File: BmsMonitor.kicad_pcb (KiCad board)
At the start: 2 copper layers, 65.5 x 98 mm, 9 parts, among them J1 Conn_01x03, J2 Conn_01x03, J3 Conn_01x04, J4 Conn_01x22, J5 Conn_01x22, U1 2365-DC-DC module, U2 ESP32-S3-DevKitC, U3 TJA1050 Module, U4 Open-Smart_3.8_LCD

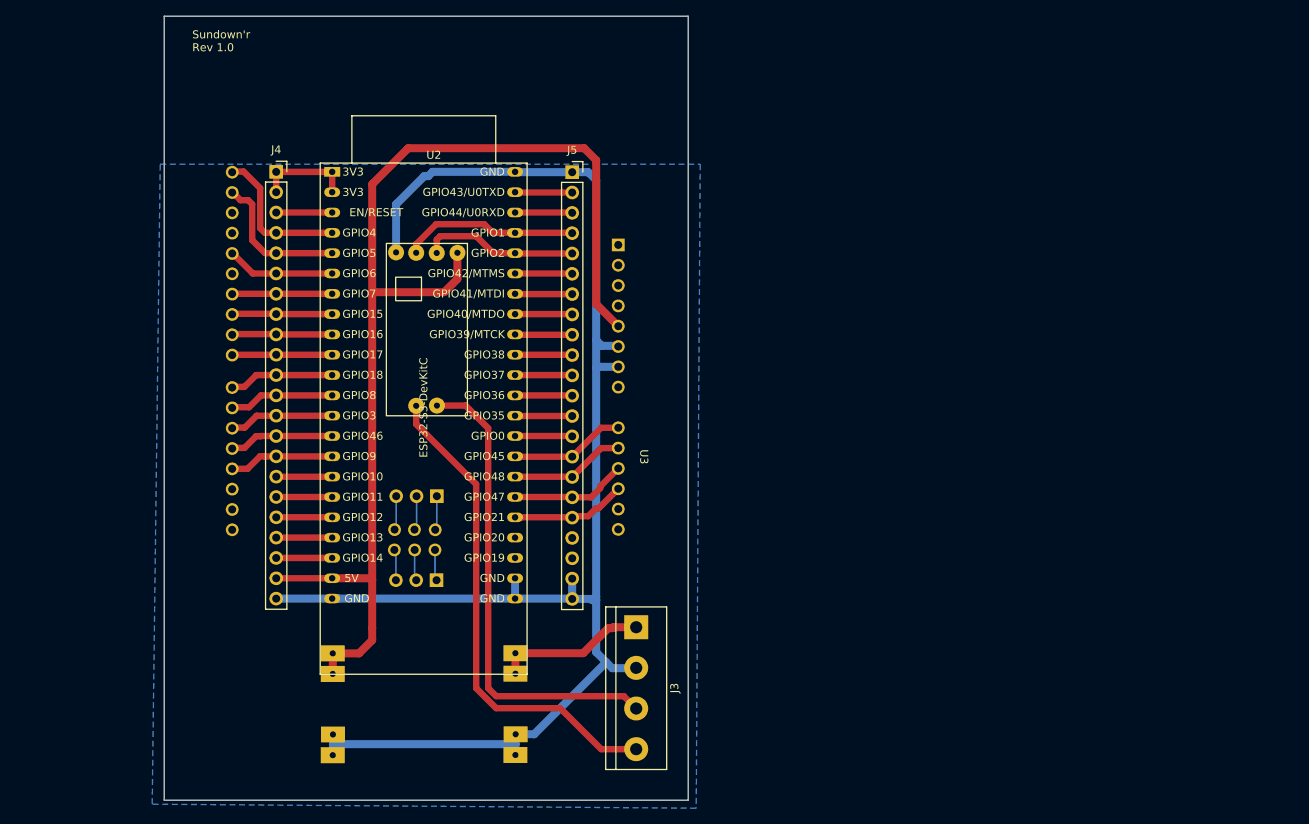
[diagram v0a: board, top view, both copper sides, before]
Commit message: BmsMonitor Ver 2.0
Changed to work with Display having a SPI variant of ILI9488
as well as a XPT2046 touch controller.

The display in question is this 3.5" display:
https://www.aliexpress.com/item/33057812377.html
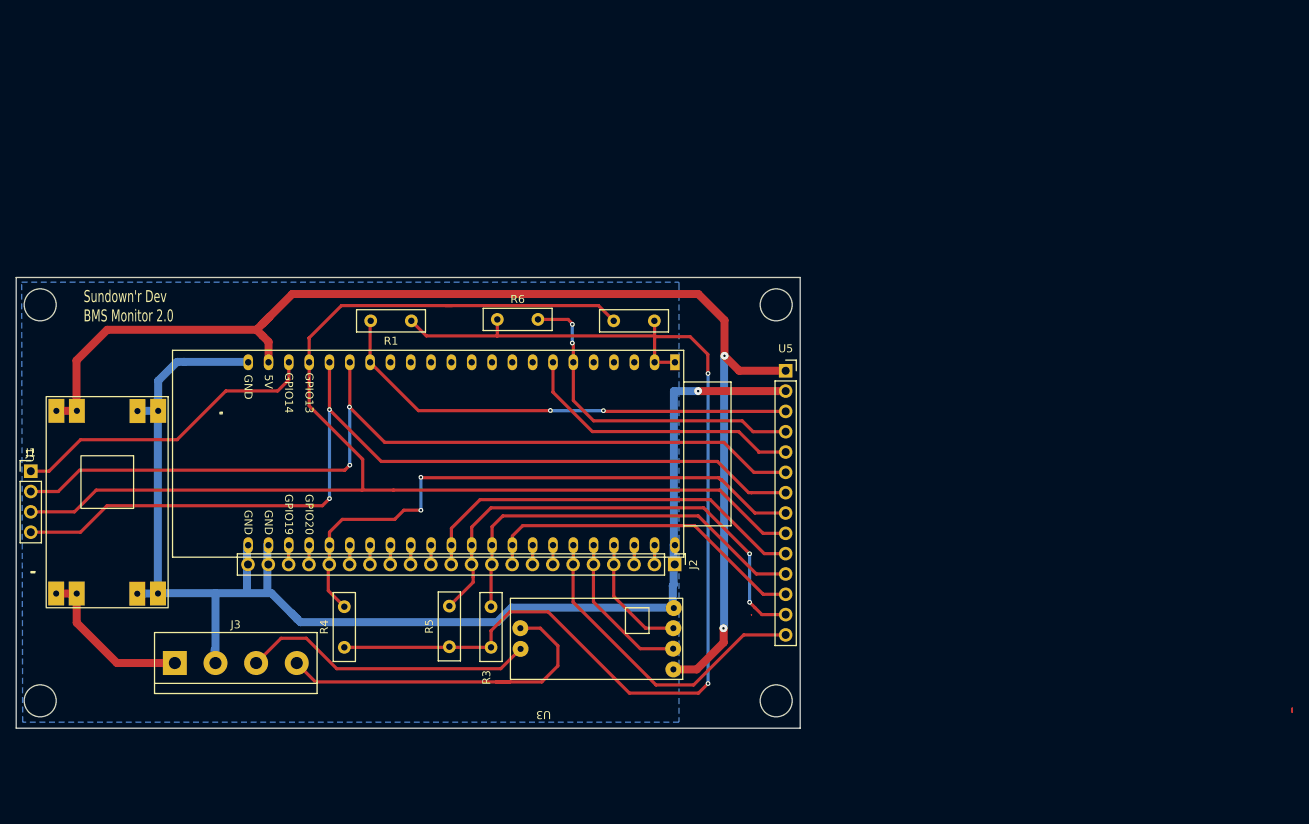
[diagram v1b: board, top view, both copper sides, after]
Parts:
- removed J4, J5: Conn_01x22, Connector_PinSocket_2.54mm:PinSocket_1x22_P2.54mm_Vertical
- removed U4: Open-Smart_3.8_LCD, Private:Open_smart_3.8_LCD
- added R1: 10K, Resistor_THT:R_Box_L8.4mm_W2.5mm_P5.08mm, F.Cu at (147.4, 68.6)
- added R2: 10K, Resistor_THT:R_Box_L8.4mm_W2.5mm_P5.08mm, F.Cu at (177.8, 68.6)
- added R3: 10K, Resistor_THT:R_Box_L8.4mm_W2.5mm_P5.08mm, F.Cu at (157.4, 109.4)
- added R4: 10K, Resistor_THT:R_Box_L8.4mm_W2.5mm_P5.08mm, F.Cu at (139.0, 109.4)
- added R5: 10K, Resistor_THT:R_Box_L8.4mm_W2.5mm_P5.08mm, F.Cu at (152.1, 109.3)
- added R6: 10K, Resistor_THT:R_Box_L8.4mm_W2.5mm_P5.08mm, F.Cu at (158.1, 68.4)
- added U5: LCD_3.5_TFT_SPI_480x320, Connector_PinSocket_2.54mm:PinSocket_1x14_P2.54mm_Vertical, F.Cu at (194.2, 74.8)
- J1: value Conn_01x03 -> Conn_01x04; footprint Connector_PinHeader_2.54mm:PinHeader_1x03_P2.54mm_Vertical -> Connector_PinHeader_2.54mm:PinHeader_1x04_P2.54mm_Vertical; moved to F.Cu
- J2: value Conn_01x03 -> Conn_01x22; footprint Connector_PinHeader_2.54mm:PinHeader_1x03_P2.54mm_Vertical -> Connector_PinHeader_2.54mm:PinHeader_1x22_P2.54mm_Vertical; moved to F.Cu
- U1: moved to F.Cu
- moved J3 57.8 mm to (117.8, 111.4), turned to 0 degrees
- moved J1 52.5 mm to (99.8, 87.4), turned to 0 degrees
- moved U2 49.0 mm to (180.3, 73.8), turned to -90 degrees
- moved U1 47.0 mm to (109.4, 91.3), turned to 90 degrees
- moved J2 30.9 mm to (180.3, 99.0), turned to -90 degrees
- moved U3 22.5 mm to (154.7, 107.0), turned to 180 degrees
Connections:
- J1 pad 1: Net-(J1-Pin_1) -> SD_CS
- J1 pad 2: Net-(J1-Pin_2) -> LCD_MOSI
- J1 pad 3: Net-(J1-Pin_3) -> LCD_MISO
- J2 pad 1: Net-(J2-Pin_1) -> GND
- U2 pad 10: LCD_D0 -> unconnected-(U2-GPIO17/ADC2_CH6-Pad10)
- U2 pad 11: LCD_D7 -> unconnected-(U2-GPIO18/ADC2_CH7-Pad11)
- U2 pad 12: LCD_D6 -> unconnected-(U2-GPIO8/ADC1_CH7-Pad12)
- U2 pad 13: SD_CS -> unconnected-(U2-GPIO3/ADC1_CH2-Pad13)
- U2 pad 14: LCD_D4 -> unconnected-(U2-GPIO46-Pad14)
- U2 pad 15: Backlight -> unconnected-(U2-GPIO9/ADC1_CH8-Pad15)
- U2 pad 16: GPIO10 -> LCD_CS
- U2 pad 17: GPIO11 -> LCD_MOSI
- U2 pad 18: GPIO12 -> LCD_CLK
- U2 pad 19: GPIO13 -> LCD_MISO
- U2 pad 20: GPIO14 -> SD_CS
- U2 pad 25: unconnected-(U2-GPIO19/USB_D--Pad25) -> unconnected-(J2-Pin_20-Pad20)
- U2 pad 26: unconnected-(U2-GPIO20/USB_D+-Pad26) -> unconnected-(J2-Pin_19-Pad19)
- U2 pad 27: LCD_CS -> Backlight
- U2 pad 28: LCD_RS -> GPIO47
- U2 pad 29: LCD_WR -> GPIO48
- U2 pad 30: LCD_RD -> GPIO45
- U2 pad 33: GPIO36 -> T_CLK
- U2 pad 34: GPIO37 -> T_MISO
- U2 pad 35: GPIO38 -> T_CS
- U2 pad 36: GPIO39 -> T_MOSI
- U2 pad 39: GPIO42 -> T_IRQ
- U2 pad 4: SCL -> unconnected-(U2-GPIO4/ADC1_CH3-Pad4)
- U2 pad 42: GPIO44 -> Net-(J2-Pin_3)
- U2 pad 43: GPIO43 -> Net-(J2-Pin_2)
- U2 pad 5: SDA -> unconnected-(U2-GPIO5/ADC1_CH4-Pad5)
- U2 pad 6: LCD_D5 -> LCD_RESET
- U2 pad 7: LCD_D3 -> LCD_DC/RS
- U2 pad 8: LCD_D2 -> unconnected-(U2-GPIO15/ADC2_CH4/32K_P-Pad8)
- U2 pad 9: LCD_D1 -> unconnected-(U2-GPIO16/ADC2_CH5/32K_N-Pad9)
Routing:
- net LCD_MISO: track 0.00 -> 161.0 mm
- net +3V3: track 12.1 -> 142.9 mm, vias 0 -> 2
- net LCD_CLK: track 0.00 -> 117.4 mm, vias 0 -> 2
- net LCD_MOSI: track 0.00 -> 112.1 mm, vias 0 -> 2
- net Backlight: track 13.2 -> 74.2 mm, vias 0 -> 2
- net T_MISO: track 0.00 -> 60.5 mm, vias 0 -> 2
- net T_CLK: track 0.00 -> 50.6 mm
- net T_CS: track 0.00 -> 50.3 mm
- net LCD_CS: track 14.5 -> 59.8 mm, vias 0 -> 2
- net LCD_RESET: track 0.00 -> 42.3 mm, vias 0 -> 2
- net T_MOSI: track 0.00 -> 41.8 mm
- net T_IRQ: track 0.00 -> 40.6 mm
- net LCD_DC/RS: track 0.00 -> 36.0 mm
- net SD_CS: track 13.2 -> 39.2 mm
- net CAN_H: track 59.6 -> 36.9 mm
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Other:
- board size 65.5 x 98 mm -> 98 x 56.3 mm
- board text added: "Sundown'r Dev BMS Monitor 2.0"
- board text added: "Sundown'r Dev BMS Monitor rev. 2.0"
- board text removed: "Sundown'r Rev 1.0"

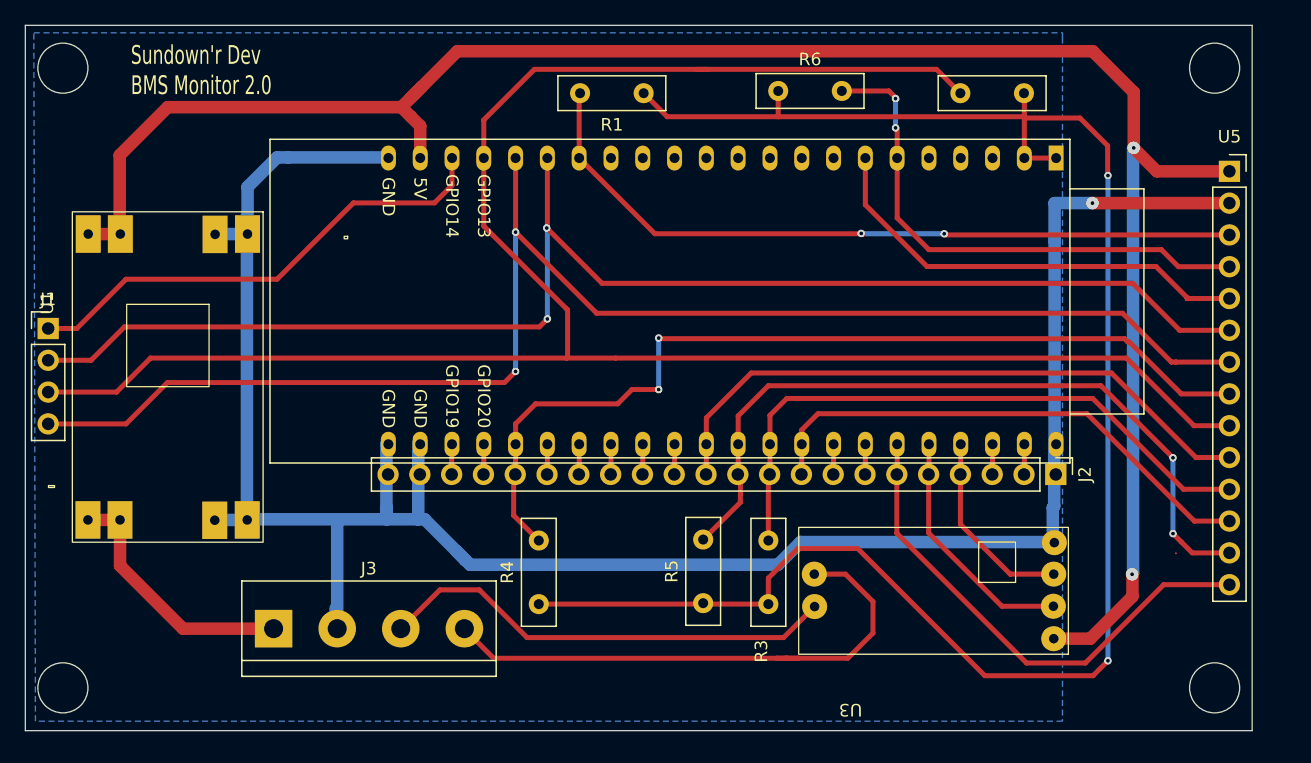
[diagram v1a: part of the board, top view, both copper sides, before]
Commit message: Use common SPI for both display and touch.
Added M12 connector for possible power and CAN
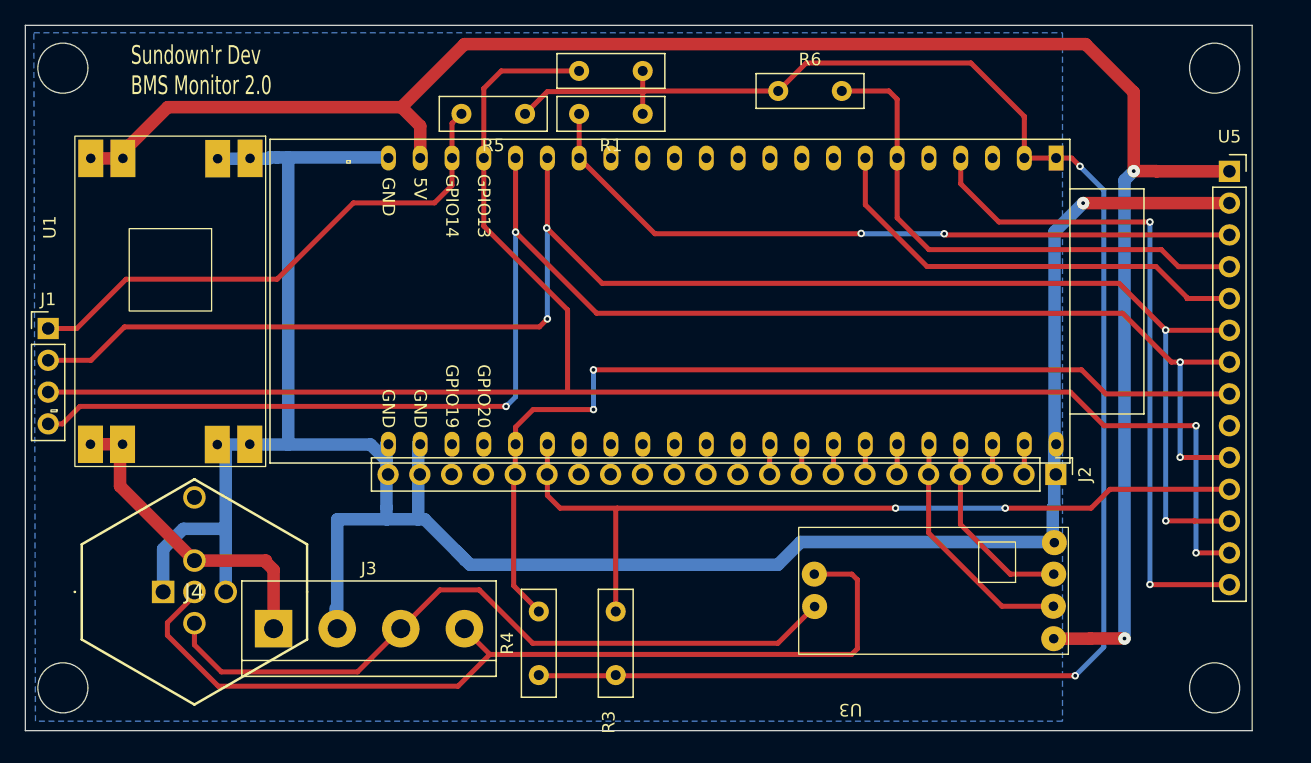
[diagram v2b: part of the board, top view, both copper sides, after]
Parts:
- added J4: MI5K101-400-A0-05, KiCad:MI5K101400A005, F.Cu at (109.0, 108.4)
- moved R5 41.6 mm to (137.9, 70.2), turned to 180 degrees
- moved R2 30.5 mm to (147.3, 66.8)
- moved R3 13.4 mm to (145.2, 115.1)
- moved U1 6.05 mm to (109.6, 85.2)
- moved R4 5.67 mm to (139.0, 115.1)
- moved R1 1.65 mm to (147.3, 70.2)
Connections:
- net GPIO40 renamed MTDO
- net GPIO41 renamed MTDI
- J2 pad 10: T_CS -> 3col_LED
- J2 pad 11: T_MISO -> unconnected-(J2-Pin_11-Pad11)
- J2 pad 12: T_CLK -> unconnected-(J2-Pin_12-Pad12)
- J2 pad 13: GPIO35 -> unconnected-(J2-Pin_13-Pad13)
- J2 pad 14: GPIO0 -> unconnected-(J2-Pin_14-Pad14)
- J2 pad 15: GPIO45 -> unconnected-(J2-Pin_15-Pad15)
- J2 pad 16: GPIO48 -> unconnected-(J2-Pin_16-Pad16)
- J2 pad 17: GPIO47 -> T_CS
- J2 pad 6: T_IRQ -> MTMS
- J2 pad 9: T_MOSI -> MTCK
- R5 pad 2: T_MISO -> SD_CS
- U2 pad 25: unconnected-(J2-Pin_20-Pad20) -> unconnected-(U2-GPIO19/USB_D--Pad25)
- U2 pad 26: unconnected-(J2-Pin_19-Pad19) -> unconnected-(U2-GPIO20/USB_D+-Pad26)
- U2 pad 28: GPIO47 -> T_CS
- U2 pad 29: GPIO48 -> unconnected-(U2-GPIO48-Pad29)
- U2 pad 30: GPIO45 -> unconnected-(U2-GPIO45-Pad30)
- U2 pad 31: GPIO0 -> BOOT
- U2 pad 32: GPIO35 -> unconnected-(U2-GPIO35-Pad32)
- U2 pad 33: T_CLK -> unconnected-(U2-GPIO36-Pad33)
- U2 pad 34: T_MISO -> unconnected-(U2-GPIO37-Pad34)
- U2 pad 35: T_CS -> 3col_LED
- U2 pad 36: T_MOSI -> MTCK
- U2 pad 39: T_IRQ -> MTMS
- U2 pad 4: unconnected-(U2-GPIO4/ADC1_CH3-Pad4) -> T_IRQ
- U5 pad 10: T_CLK -> LCD_CLK
- U5 pad 12: T_MOSI -> LCD_MOSI
- U5 pad 13: T_MISO -> LCD_MISO
- U5 pad 9: LCD_MISO -> unconnected-(U5-LCD_MISO-Pad9)
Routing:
- net T_MISO: track 60.5 -> 0.00 mm, vias 2 -> 0
- net T_CLK: track 50.6 -> 0.00 mm
- net T_MOSI: track 41.8 -> 0.00 mm
- net CAN_L: track 44.5 -> 74.4 mm
- net CAN_H: track 36.9 -> 57.9 mm
- net LCD_MISO: track 161.0 -> 140.6 mm, vias 0 -> 2
- net LCD_MOSI: track 112.1 -> 132.4 mm, vias 2 -> 4
- net GND: track 175.9 -> 194.3 mm
- net T_CS: track 50.3 -> 67.9 mm, vias 0 -> 2
- net T_IRQ: track 40.6 -> 53.7 mm, vias 0 -> 2
- net LCD_CLK: track 117.4 -> 130.2 mm, vias 2 -> 4
- net +5V: track 157.0 -> 150.8 mm
- net +12V: track 20.6 -> 25.5 mm
- net SD_CS: track 39.2 -> 43.0 mm
- net Backlight: track 74.2 -> 77.2 mm
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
